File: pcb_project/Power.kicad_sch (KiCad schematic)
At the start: 44 parts, among them IC1 TPS54325PWPR, IC2 TPS54294PWPR, J5 USB_B_Micro

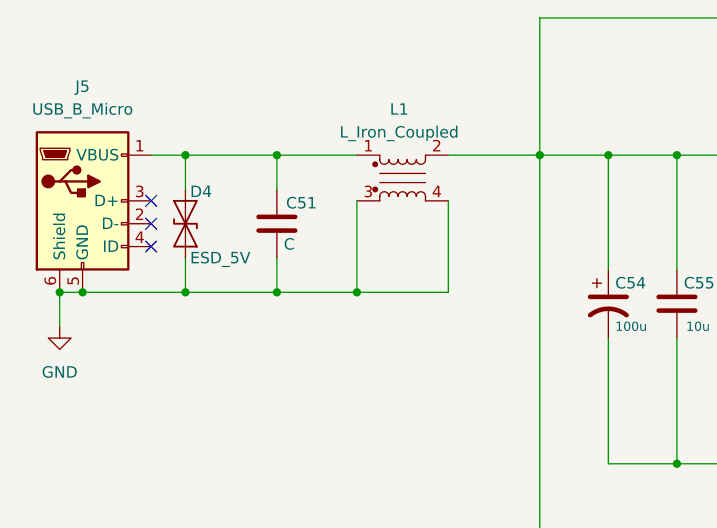
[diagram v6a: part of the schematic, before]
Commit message: Add most footprints, missing some inductors and 3 buttons
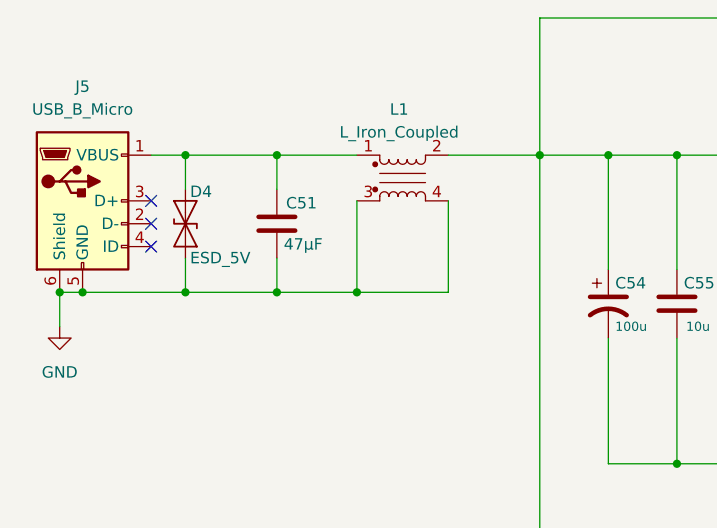
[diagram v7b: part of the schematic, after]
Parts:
- C51: value C -> 47μF; footprint (none) -> Capacitor_SMD:C_1210_3225Metric_Pad1.33x2.70mm_HandSolder
- C52, C53, C55, C56, C65, C66, C68, C69, C70: footprint (none) -> Capacitor_SMD:C_1206_3216Metric_Pad1.33x1.80mm_HandSolder
- C54: footprint (none) -> Capacitor_SMD:C_1210_3225Metric_Pad1.33x2.70mm_HandSolder
- C57, C58, C59, C60, C62, C63, C67: footprint (none) -> Capacitor_SMD:C_0603_1608Metric_Pad1.08x0.95mm_HandSolder
- C61, C64: footprint (none) -> Capacitor_SMD:C_0805_2012Metric_Pad1.18x1.45mm_HandSolder
- FB2, FB3: footprint (none) -> Inductor_SMD:L_0805_2012Metric_Pad1.15x1.40mm_HandSolder
- IC2: footprint (none) -> Project_Footprints:SOP65P640X120-15N
- J5: footprint (none) -> Connector_USB:USB_Micro-B_Amphenol_10103594-0001LF_Horizontal
- JP1, JP2, JP3, JP4, JP5: footprint (none) -> Jumper:Jumper_Harwin_S1621_P10.9mm
- L1: footprint (none) -> Inductor_SMD:L_CommonModeChoke_Coilcraft_0805USB
- L2: footprint (none) -> Inductor_SMD:L_Bourns-SRN4018
- R44, R45, R46, R47, R48, R49, R50, R51, R52: footprint (none) -> Resistor_SMD:R_0805_2012Metric_Pad1.20x1.40mm_HandSolder
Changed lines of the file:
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@@
 			)
 		)
-		(property "Footprint" ""
+		(property "Footprint" "Capacitor_SMD:C_0603_1608Metric_Pad1.08x0.95mm_HandSolder"
 			(at 166.37 42.2148 0)
 			(effects
@@
 			)
 		)
-		(property "Footprint" ""
+		(property "Footprint" "Capacitor_SMD:C_0603_1608Metric_Pad1.08x0.95mm_HandSolder"
 			(at 186.3852 111.76 0)
 			(effects
@@
 			)
 		)
-		(property "Footprint" ""
+		(property "Footprint" "Inductor_SMD:L_Bourns-SRN4018"
 			(at 101.6 118.11 0)
 			(effects
@@
 			)
 		)
-		(property "Footprint" ""
+		(property "Footprint" "Capacitor_SMD:C_0603_1608Metric_Pad1.08x0.95mm_HandSolder"
 			(at 113.9952 55.88 0)
 			(effects
@@
 			)
 		)
-		(property "Footprint" ""
+		(property "Footprint" "Capacitor_SMD:C_1206_3216Metric_Pad1.33x1.80mm_HandSolder"
 			(at 108.9152 111.76 0)
 			(effects
@@
 			)
 		)
-		(property "Footprint" ""
+		(property "Footprint" "Resistor_SMD:R_0805_2012Metric_Pad1.20x1.40mm_HandSolder"
 			(at 218.948 137.16 90)
 			(effects
@@
 			)
 		)
-		(property "Footprint" ""
+		(property "Footprint" "Resistor_SMD:R_0805_2012Metric_Pad1.20x1.40mm_HandSolder"
 			(at 163.322 133.35 90)
 			(effects
@@
 			)
 		)
-		(property "Footprint" ""
+		(property "Footprint" "Capacitor_SMD:C_0805_2012Metric_Pad1.18x1.45mm_HandSolder"
 			(at 159.7152 67.31 0)
 			(effects
@@
 			)
 		)
-		(property "Footprint" ""
+		(property "Footprint" "Capacitor_SMD:C_1206_3216Metric_Pad1.33x1.80mm_HandSolder"
 			(at 186.3852 62.23 0)
 			(effects
@@
 			)
 		)
-		(property "Footprint" ""
+		(property "Footprint" "Resistor_SMD:R_0805_2012Metric_Pad1.20x1.40mm_HandSolder"
 			(at 75.692 124.46 90)
 			(effects
@@
 			)
 		)
-		(property "Footprint" ""
+		(property "Footprint" "Inductor_SMD:L_0805_2012Metric_Pad1.15x1.40mm_HandSolder"
 			(at 232.41 73.152 90)
 			(effects
@@
 			)
 		)
-		(property "Footprint" ""
+		(property "Footprint" "Project_Footprints:SOP65P640X120-15N"
 			(at 154.94 202.87 0)
 			(effects
@@
 			)
 		)
-		(property "Footprint" ""
+		(property "Footprint" "Capacitor_SMD:C_0603_1608Metric_Pad1.08x0.95mm_HandSolder"
 			(at 120.65 116.5352 0)
 			(effects
@@
 			)
 		)
-		(property "Footprint" ""
+		(property "Footprint" "Jumper:Jumper_Harwin_S1621_P10.9mm"
 			(at 252.73 85.09 0)
 			(effects
@@
 			)
 		)
-		(property "Footprint" ""
+		(property "Footprint" "Capacitor_SMD:C_0805_2012Metric_Pad1.18x1.45mm_HandSolder"
 			(at 172.4152 137.16 0)
 			(effects
@@
 			)
 		)
-		(property "Footprint" ""
+		(property "Footprint" "Connector_USB:USB_Micro-B_Amphenol_10103594-0001LF_Horizontal"
 			(at 43.18 41.91 0)
 			(effects
@@
 			)
 		)
-		(property "Footprint" ""
+		(property "Footprint" "Inductor_SMD:L_0805_2012Metric_Pad1.15x1.40mm_HandSolder"
 			(at 228.6 119.888 90)
 			(effects
@@
 			)
 		)
-		(property "Footprint" ""
+		(property "Footprint" "Capacitor_SMD:C_1206_3216Metric_Pad1.33x1.80mm_HandSolder"
 			(at 210.5152 128.27 0)
 			(effects
@@
 			)
 		)
-		(property "Footprint" ""
+		(property "Footprint" "Inductor_SMD:L_CommonModeChoke_Coilcraft_0805USB"
 			(at 74.93 38.1 0)
 			(effects
@@
 			)
 		)
-		(property "Footprint" ""
+		(property "Footprint" "Jumper:Jumper_Harwin_S1621_P10.9mm"
 			(at 252.73 74.93 0)
 			(effects
@@
 			)
 		)
-		(property "Footprint" ""
+		(property "Footprint" "Jumper:Jumper_Harwin_S1621_P10.9mm"
 			(at 252.73 118.11 0)
 			(effects
@@
 			)
 		)
-		(property "Footprint" ""
+		(property "Footprint" "Capacitor_SMD:C_1206_3216Metric_Pad1.33x1.80mm_HandSolder"
 			(at 194.0052 62.23 0)
 			(effects
@@
 			)
 		)
-		(property "Footprint" ""
+		(property "Footprint" "Capacitor_SMD:C_1206_3216Metric_Pad1.33x1.80mm_HandSolder"
 			(at 84.1248 128.27 0)
 			(effects
@@
 			)
 		)
-		(property "Footprint" ""
+		(property "Footprint" "Capacitor_SMD:C_0603_1608Metric_Pad1.08x0.95mm_HandSolder"
 			(at 116.5352 111.76 0)
 			(effects
@@
 			)
 		)
-		(property "Footprint" ""
+		(property "Footprint" "Capacitor_SMD:C_1206_3216Metric_Pad1.33x1.80mm_HandSolder"
 			(at 178.7652 111.76 0)
 			(effects
@@
 			)
 		)
-		(property "Footprint" ""
+		(property "Footprint" "Resistor_SMD:R_0805_2012Metric_Pad1.20x1.40mm_HandSolder"
 			(at 75.692 137.16 90)
 			(effects
@@
 			)
 		)
-		(property "Footprint" ""
+		(property "Footprint" "Jumper:Jumper_Harwin_S1621_P10.9mm"
 			(at 252.73 109.22 0)
 			(effects
@@
 			)
 		)
-		(property "Footprint" ""
+		(property "Footprint" "Capacitor_SMD:C_0603_1608Metric_Pad1.08x0.95mm_HandSolder"
 			(at 121.6152 55.88 0)
 			(effects
@@
 			)
 		)
-		(property "Footprint" ""
+		(property "Footprint" "Capacitor_SMD:C_1210_3225Metric_Pad1.33x2.70mm_HandSolder"
 			(at 97.79 52.07 0)
 			(effects
@@
 			)
 		)
-		(property "Footprint" ""
+		(property "Footprint" "Resistor_SMD:R_0805_2012Metric_Pad1.20x1.40mm_HandSolder"
 			(at 162.56 54.102 90)
 			(effects
@@
 			)
 		)
-		(property "Footprint" ""
+		(property "Footprint" "Capacitor_SMD:C_1206_3216Metric_Pad1.33x1.80mm_HandSolder"
 			(at 106.3752 55.88 0)
 			(effects
@@
 			)
 		)
-		(property "Footprint" ""
+		(property "Footprint" "Resistor_SMD:R_0805_2012Metric_Pad1.20x1.40mm_HandSolder"
 			(at 181.61 44.958 90)
 			(effects
@@
 			)
 		)
-		(property "Footprint" ""
+		(property "Footprint" "Resistor_SMD:R_0805_2012Metric_Pad1.20x1.40mm_HandSolder"
 			(at 173.99 44.958 90)
 			(effects
@@
 			)
 		)
-		(property "Footprint" ""
+		(property "Footprint" "Jumper:Jumper_Harwin_S1621_P10.9mm"
 			(at 252.73 93.98 0)
 			(effects
@@
 			)
 		)
-		(property "Footprint" ""
+		(property "Footprint" "Capacitor_SMD:C_0603_1608Metric_Pad1.08x0.95mm_HandSolder"
 			(at 166.37 116.5352 0)
 			(effects
@@
 			)
 		)
-		(property "Footprint" ""
+		(property "Footprint" "Capacitor_SMD:C_1206_3216Metric_Pad1.33x1.80mm_HandSolder"
 			(at 202.8952 128.27 0)
 			(effects
@@
 			)
 		)
-		(property "Footprint" ""
+		(property "Footprint" "Resistor_SMD:R_0805_2012Metric_Pad1.20x1.40mm_HandSolder"
 			(at 218.948 124.46 90)
 			(effects
@@
 			)
 		)
-		(property "Footprint" ""
+		(property "Footprint" "Capacitor_SMD:C_1206_3216Metric_Pad1.33x1.80mm_HandSolder"
 			(at 91.7448 128.27 0)
 			(effects
@@
 			)
 		)
-		(property "Value" "C"
+		(property "Value" "47μF"
 			(at 61.722 45.466 0)
 			(effects
@@
 			)
 		)
-		(property "Footprint" ""
+		(property "Footprint" "Capacitor_SMD:C_1210_3225Metric_Pad1.33x2.70mm_HandSolder"
 			(at 61.9252 46.99 0)
 			(effects
@@
 			)
 		)
-		(property "Footprint" ""
+		(property "Footprint" "Resistor_SMD:R_0805_2012Metric_Pad1.20x1.40mm_HandSolder"
 			(at 236.22 119.888 90)
 			(effects

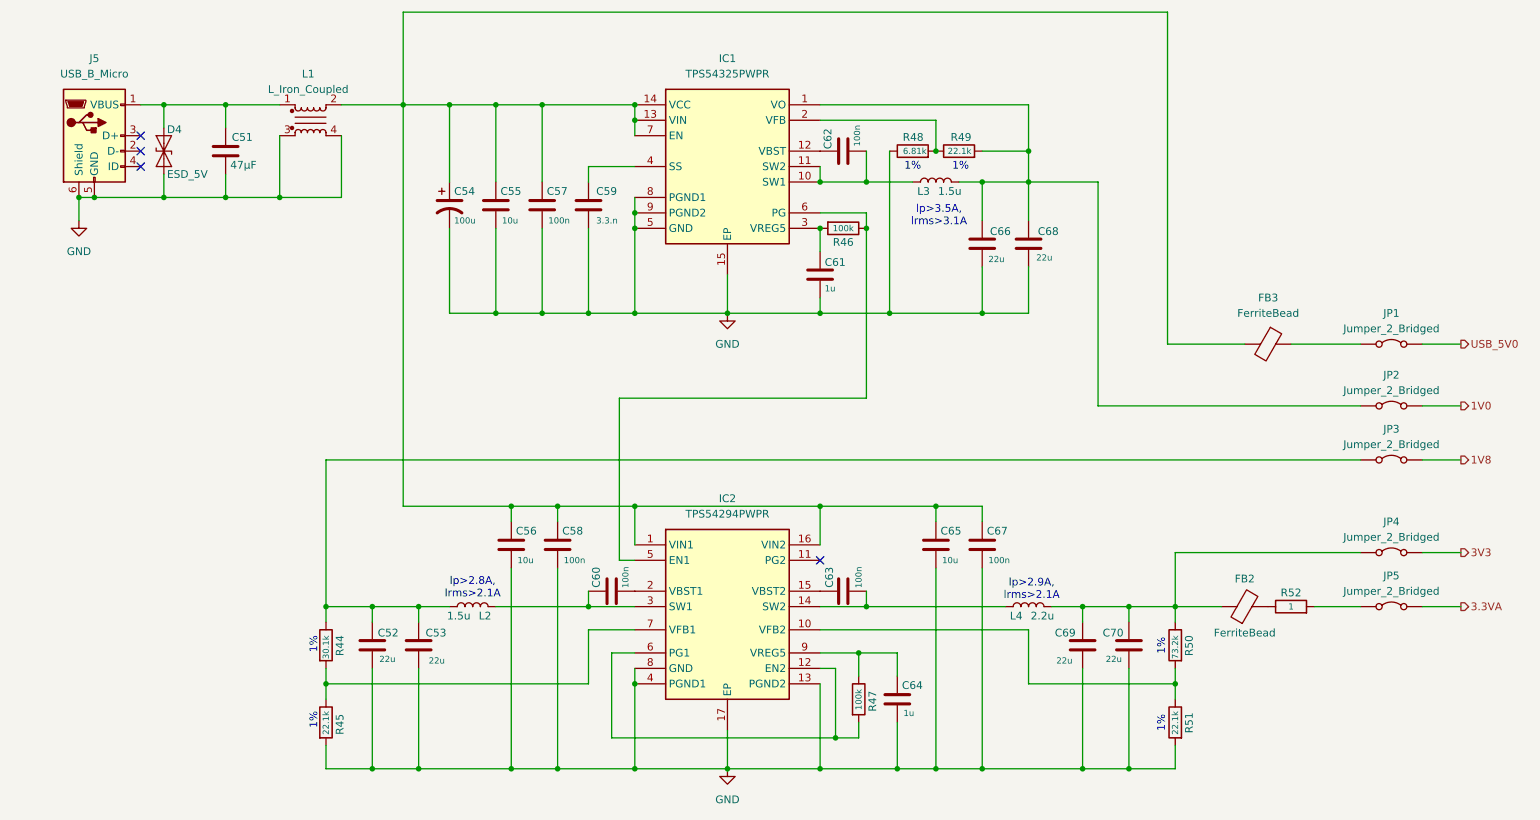
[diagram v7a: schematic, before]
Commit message: Update power connectors
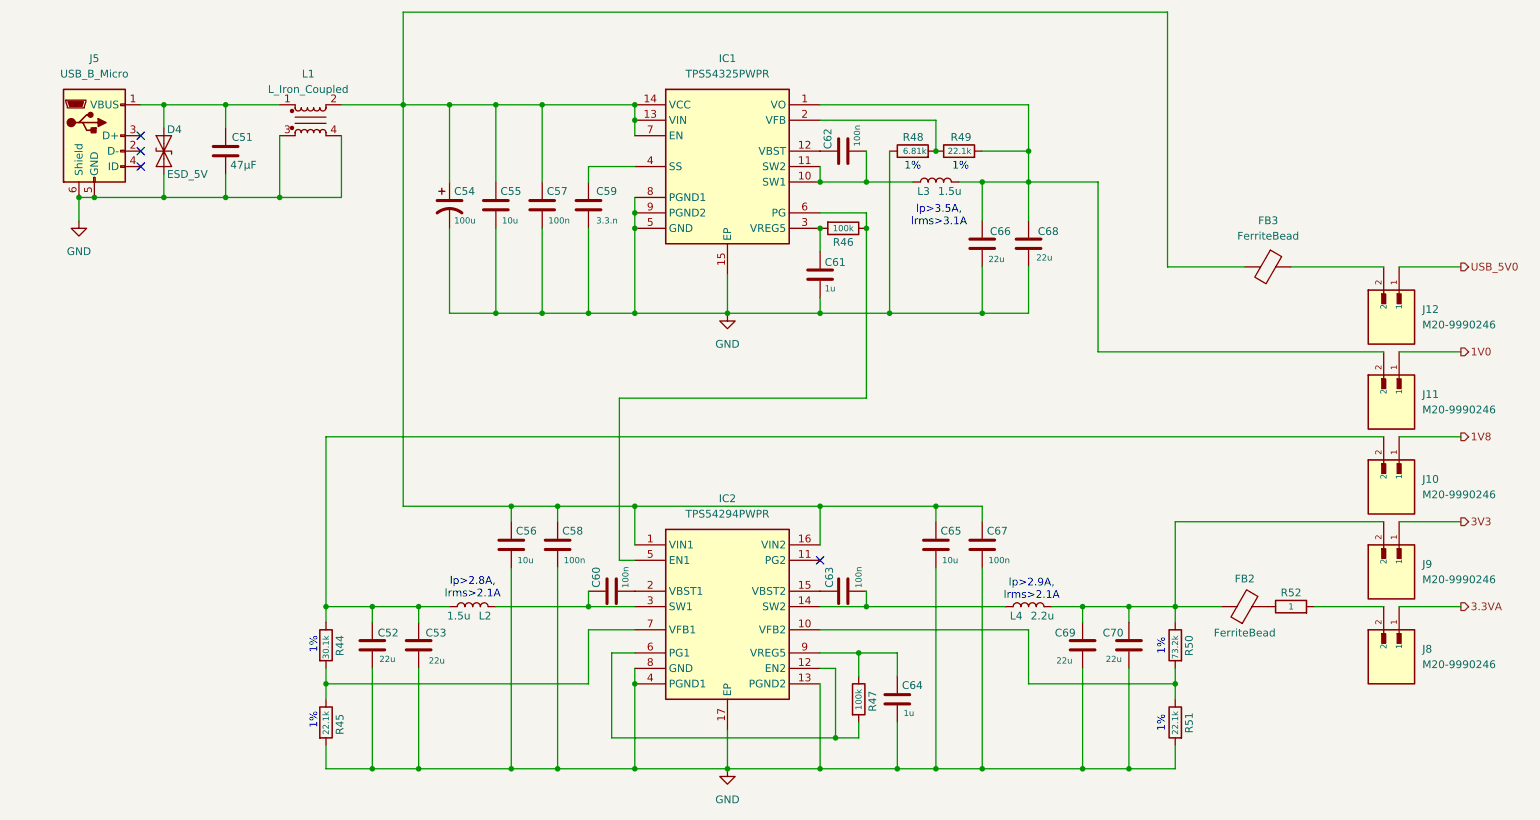
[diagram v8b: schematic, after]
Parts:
- removed JP1, JP2, JP3, JP4, JP5: Jumper_2_Bridged, Jumper:Jumper_Harwin_S1621_P10.9mm, symbol Jumper:Jumper_2_Bridged
- added J10, J11, J12, J8, J9: M20-9990246, M20-9990246:HARWIN_M20-9990246, symbol M20-9990246:M20-9990246
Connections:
- net 1V0: now also J11.1
- net 1V8: now also J10.1
- net 3.3VA: now also J8.1
- net 3V3: now also J9.1
- net USB_5V0: now also J12.1
- net at C52.1, C53.1, L2.2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: now also J10.2
- net at C69.1, C70.1, FB2.1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: now also J9.2
- net at C66.1, C68.1, IC1.1 (VO)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: now also J11.2
- net at FB3.1: now also J12.2
- net at R52.2: now also J8.2
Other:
- moved on the sheet: FB3
